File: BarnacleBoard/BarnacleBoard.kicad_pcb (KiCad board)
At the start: 2 copper layers, 82.6 x 63.4 mm, 114 parts, among them J1 Conn_02x35_Top_Bottom, J11 Connector_Breadboard, J12 Conn_02x03_Top_Bottom, J13 Conn_02x03_Top_Bottom, J14 Conn_01x06, J15 Conn_01x01, J2 pad_sense_1, J3 pad_sense_30, J4 pad_sense_60, J5 pad_sense_31, J6 Conn_02x35_Top_Bottom

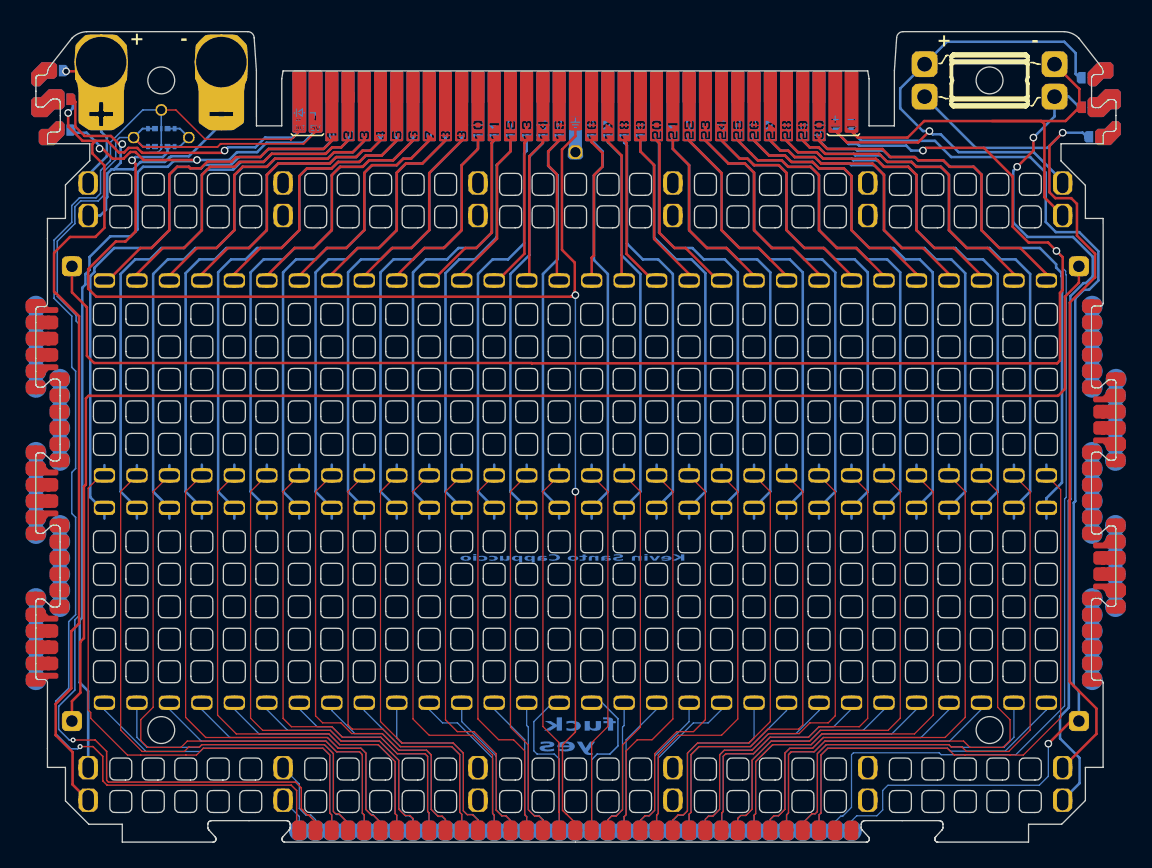
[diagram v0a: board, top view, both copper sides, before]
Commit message: add wigs
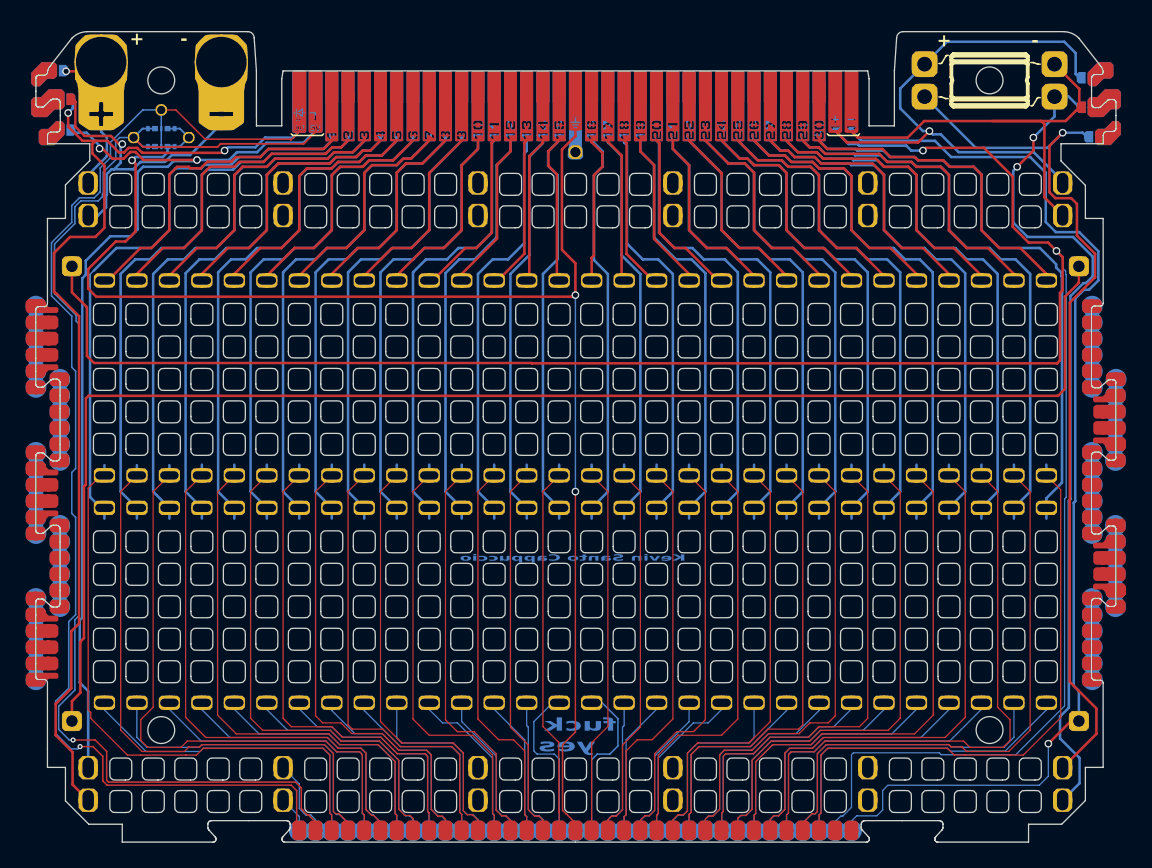
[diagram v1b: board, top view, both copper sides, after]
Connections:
- net BOT_NEG renamed BOT_RAIL_NEG
- net BOT_POS renamed BOT_RAIL_POS
- net LED_GND renamed GND
- net LED_IN renamed LED_DAT
- net Net-(J1-Pin_1) renamed 1
- net Net-(J1-Pin_10) renamed 10
- net Net-(J1-Pin_11) renamed 11
- net Net-(J1-Pin_12) renamed 12
- net Net-(J1-Pin_13) renamed 13
- net Net-(J1-Pin_14) renamed 14
- net Net-(J1-Pin_15) renamed 15
- net Net-(J1-Pin_16) renamed 16
- net Net-(J1-Pin_17) renamed 17
- net Net-(J1-Pin_18) renamed 18
- net Net-(J1-Pin_19) renamed 19
- net Net-(J1-Pin_2) renamed 2
- net Net-(J1-Pin_20) renamed 20
- net Net-(J1-Pin_21) renamed 21
- net Net-(J1-Pin_22) renamed 22
- net Net-(J1-Pin_23) renamed 23
- net Net-(J1-Pin_24) renamed 24
- net Net-(J1-Pin_25) renamed 25
- net Net-(J1-Pin_26) renamed 26
- net Net-(J1-Pin_27) renamed 27
- net Net-(J1-Pin_28) renamed 28
- net Net-(J1-Pin_29) renamed 29
- net Net-(J1-Pin_3) renamed 3
- net Net-(J1-Pin_30) renamed 30
- net Net-(J1-Pin_31) renamed 31
- net Net-(J1-Pin_32) renamed 32
- net Net-(J1-Pin_33) renamed 33
- net Net-(J1-Pin_34) renamed 34
- net Net-(J1-Pin_35) renamed 35
- net Net-(J1-Pin_36) renamed 36
- net Net-(J1-Pin_37) renamed 37
- net Net-(J1-Pin_38) renamed 38
- net Net-(J1-Pin_39) renamed 39
- net Net-(J1-Pin_4) renamed 4
- net Net-(J1-Pin_40) renamed 40
- net Net-(J1-Pin_41) renamed 41
- net Net-(J1-Pin_42) renamed 42
- net Net-(J1-Pin_43) renamed 43
- net Net-(J1-Pin_44) renamed 44
- net Net-(J1-Pin_45) renamed 45
- net Net-(J1-Pin_46) renamed 46
- net Net-(J1-Pin_47) renamed 47
- net Net-(J1-Pin_48) renamed 48
- net Net-(J1-Pin_49) renamed 49
- net Net-(J1-Pin_5) renamed 5
- net Net-(J1-Pin_50) renamed 50
- net Net-(J1-Pin_51) renamed 51
- net Net-(J1-Pin_52) renamed 52
- net Net-(J1-Pin_53) renamed 53
- net Net-(J1-Pin_54) renamed 54
- net Net-(J1-Pin_55) renamed 55
- net Net-(J1-Pin_56) renamed 56
- net Net-(J1-Pin_57) renamed 57
- net Net-(J1-Pin_58) renamed 58
- net Net-(J1-Pin_59) renamed 59
- net Net-(J1-Pin_6) renamed 6
- net Net-(J1-Pin_60) renamed 60
- net Net-(J1-Pin_65) renamed PASS
- net Net-(J1-Pin_7) renamed 7
- net Net-(J1-Pin_8) renamed 8
- net Net-(J1-Pin_9) renamed 9
- net PAD_SENSE_IN renamed SENSE_TOP
- net PAD_SENSE_OUT renamed SENSE_BOTTOM
- net TOP_NEG renamed TOP_RAIL_NEG
- net TOP_POS renamed TOP_RAIL_POS
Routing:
- net LED_DAT: track 96.8 -> 95.6 mm
- net 31: track 70.7 -> 71.5 mm
